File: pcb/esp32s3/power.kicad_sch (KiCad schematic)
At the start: 15 parts, among them J1 USB_C_Receptacle_USB2.0_14P, J2 Battery, Q1 DMG3414U, U2 AZ1117-3.3, U3 USBLC6-2SC6, U4 MCP73831-2-OT

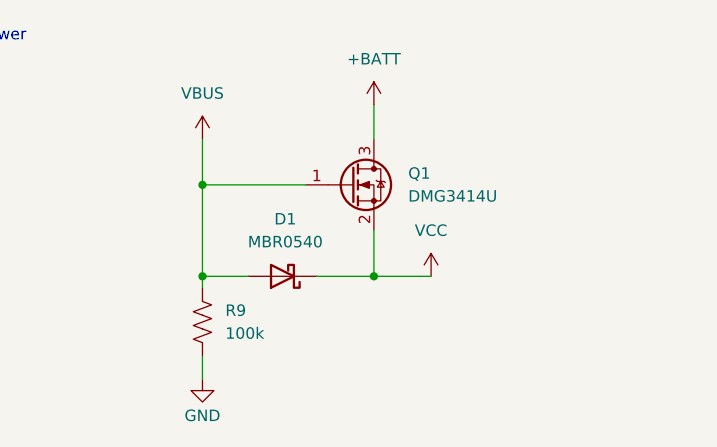
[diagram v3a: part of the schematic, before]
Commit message: fix power circuit
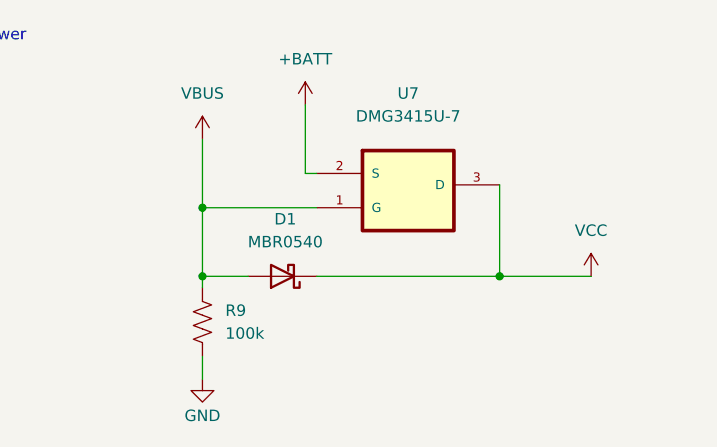
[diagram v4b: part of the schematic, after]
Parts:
- removed Q1: DMG3414U, Package_TO_SOT_SMD:SOT-23, symbol Transistor_FET:DMG3414U
- added U7: DMG3415U-7, DMG3415:SOT95P240X105-3N, symbol DMG3415U-7:DMG3415U-7
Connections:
- net +BATT: now also U7.2 (S)
- net VBUS: now also U7.1 (G)
- net VCC: now also U7.3 (D)
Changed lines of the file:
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@@
 	)
 	(junction
-		(at 248.92 40.64)
-		(diameter 0)
-		(color 0 0 0 0)
-	)
-	(junction
 		(at 57.15 30.48)
 		(diameter 0)
@@
 	)
 	(junction
-		(at 83.82 96.52)
+		(at 262.89 40.64)
+		(diameter 0)
+		(color 0 0 0 0)
+	)
+	(junction
+		(at 229.87 33.02)
 		(diameter 0)
 		(color 0 0 0 0)
 	)
 	(junction
-		(at 229.87 30.48)
+		(at 83.82 96.52)
 		(diameter 0)
 		(color 0 0 0 0)
@@
 	(wire
 		(pts
+			(xy 262.89 40.64) (xy 273.05 40.64)
+		)
+		(stroke
+			(width 0)
+			(type default)
+		)
+	)
+	(wire
+		(pts
 			(xy 234.95 83.82) (xy 240.03 83.82)
 		)
@@
 		)
 	)
+	(wire
+		(pts
+			(xy 229.87 33.02) (xy 229.87 40.64)
+		)
+		(stroke
+			(width 0)
+			(type default)
+		)
+	)
 	(polyline
 		(pts
@@
 	(wire
 		(pts
-			(xy 229.87 25.4) (xy 229.87 30.48)
+			(xy 229.87 25.4) (xy 229.87 33.02)
 		)
 		(stroke
@@
 	(wire
 		(pts
-			(xy 229.87 30.48) (xy 241.3 30.48)
+			(xy 229.87 33.02) (xy 242.57 33.02)
 		)
 		(stroke
@@
 	(wire
 		(pts
-			(xy 248.92 40.64) (xy 248.92 35.56)
-		)
-		(stroke
-			(width 0)
-			(type default)
-		)
-	)
-	(wire
-		(pts
 			(xy 86.36 87.63) (xy 86.36 88.9)
 		)
@@
 	(wire
 		(pts
-			(xy 248.92 40.64) (xy 255.27 40.64)
+			(xy 242.57 40.64) (xy 262.89 40.64)
 		)
 		(stroke
@@
 		)
 	)
-	(wire
+	(polyline
 		(pts
-			(xy 229.87 30.48) (xy 229.87 40.64)
+			(xy 11.938 59.944) (xy 79.756 59.944)
 		)
 		(stroke
@@
 	(wire
 		(pts
-			(xy 242.57 40.64) (xy 248.92 40.64)
+			(xy 241.3 29.21) (xy 242.57 29.21)
 		)
 		(stroke
@@
 		)
 	)
-	(polyline
+	(wire
 		(pts
-			(xy 11.938 59.944) (xy 79.756 59.944)
+			(xy 262.89 30.48) (xy 262.89 40.64)
 		)
 		(stroke
@@
 	(wire
 		(pts
-			(xy 248.92 21.59) (xy 248.92 25.4)
+			(xy 241.3 21.59) (xy 241.3 29.21)
 		)
 		(stroke
@@
 	)
 	(symbol
+		(lib_id "DMG3415U-7:DMG3415U-7")
+		(at 252.73 30.48 0)
+		(unit 1)
+		(exclude_from_sim no)
+		(in_bom yes)
+		(on_board yes)
+		(dnp no)
+		(fields_autoplaced yes)
+		(property "Reference" "U7"
+			(at 252.73 20.32 0)
+			(effects
+				(font
+					(size 1.27 1.27)
+				)
+			)
+		)
+		(property "Value" "DMG3415U-7"
+			(at 252.73 22.86 0)
+			(effects
+				(font
+					(size 1.27 1.27)
+				)
+			)
+		)
+		(property "Footprint" "DMG3415:SOT95P240X105-3N"
+			(at 252.73 30.48 0)
+			(effects
+				(font
+					(size 1.27 1.27)
+				)
+				(justify bottom)
+				(hide yes)
+			)
+		)
+		(property "Datasheet" ""
+			(at 252.73 30.48 0)
+			(effects
+				(font
+					(size 1.27 1.27)
+				)
+				(hide yes)
+			)
+		)
+		(property "Description" ""
+			(at 252.73 30.48 0)
+			(effects
+				(font
+					(size 1.27 1.27)
+				)
+				(hide yes)
+			)
+		)
+		(property "MPN" "DMG3415U-7"
+			(at 252.73 30.48 0)
+			(effects
+				(font
+					(size 1.27 1.27)
+				)
+				(justify bottom)
+				(hide yes)
+			)
+		)
+		(property "OC_FARNELL" "1843688"
+			(at 252.73 30.48 0)
+			(effects
+				(font
+					(size 1.27 1.27)
+				)
+				(justify bottom)
+				(hide yes)
+			)
+		)
+		(property "OC_NEWARK" "12T2026"
+			(at 252.73 30.48 0)
+			(effects
+				(font
+					(size 1.27 1.27)
+				)
+				(justify bottom)
+				(hide yes)
+			)
+		)
+		(property "SUPPLIER" "Diodes Inc"
+			(at 252.73 30.48 0)
+			(effects
+				(font
+					(size 1.27 1.27)
+				)
+				(justify bottom)
+				(hide yes)
+			)
+		)
+		(property "PACKAGE" "SOT-23-3"
+			(at 252.73 30.48 0)
+			(effects
+				(font
+					(size 1.27 1.27)
+				)
+				(justify bottom)
+				(hide yes)
+			)
+		)
+		(pin "1"
+		)
+		(pin "2"
+		)
+		(pin "3"
+		)
+		(instances
+			(project "esp32s3"
+				(path "/834edf73-57a5-43b4-ab36-0b077e93e6d5/ae5309e0-349d-45c3-b1b4-6edffcac73ca"
+					(reference "U7")
+					(unit 1)
+				)
+			)
+		)
+	)
+	(symbol
 		(lib_id "Device:R_US")
 		(at 86.36 92.71 0)
@@
 	(symbol
 		(lib_id "power:VCC")
-		(at 255.27 40.64 0)
+		(at 273.05 40.64 0)
 		(unit 1)
 		(exclude_from_sim no)
@@
 		(fields_autoplaced yes)
 		(property "Reference" "#PWR034"
-			(at 255.27 44.45 0)
+			(at 273.05 44.45 0)
 			(effects
 				(font
@@
 		)
 		(property "Value" "VCC"
-			(at 255.27 35.56 0)
+			(at 273.05 35.56 0)
 			(effects
 				(font
@@
 		)
 		(property "Footprint" ""
-			(at 255.27 40.64 0)
+			(at 273.05 40.64 0)
 			(effects
 				(font
@@
 		)
 		(property "Datasheet" ""
-			(at 255.27 40.64 0)
+			(at 273.05 40.64 0)
 			(effects
 				(font
@@
 		)
 		(property "Description" "Power symbol creates a global label with name \"VCC\""
-			(at 255.27 40.64 0)
+			(at 273.05 40.64 0)
 			(effects
 				(font
@@
 	(symbol
 		(lib_id "power:+BATT")
-		(at 248.92 21.59 0)
+		(at 241.3 21.59 0)
 		(unit 1)
 		(exclude_from_sim no)
@@
 		(fields_autoplaced yes)
 		(property "Reference" "#PWR033"
-			(at 248.92 25.4 0)
+			(at 241.3 25.4 0)
 			(effects
 				(font
@@
 		)
 		(property "Value" "+BATT"
-			(at 248.92 16.51 0)
+			(at 241.3 16.51 0)
 			(effects
 				(font
@@
 		)
 		(property "Footprint" ""
-			(at 248.92 21.59 0)
+			(at 241.3 21.59 0)
 			(effects
 				(font
@@
 		)
 		(property "Datasheet" ""
-			(at 248.92 21.59 0)
+			(at 241.3 21.59 0)
 			(effects
 				(font
@@
 		)
 		(property "Description" "Power symbol creates a global label with name \"+BATT\""
-			(at 248.92 21.59 0)
+			(at 241.3 21.59 0)
 			(effects
 				(font
@@
 					(unit 1)
 				)
-			)
-		)
-	)
-	(symbol
-		(lib_id "Transistor_FET:DMG3414U")
-		(at 246.38 30.48 0)
-		(unit 1)
-		(exclude_from_sim no)
-		(in_bom yes)
-		(on_board yes)
-		(dnp no)
-		(fields_autoplaced yes)
-		(property "Reference" "Q1"
-			(at 252.73 29.2099 0)
-			(effects
-				(font
-					(size 1.27 1.27)
-				)
-				(justify left)
-			)
-		)
-		(property "Value" "DMG3414U"
-			(at 252.73 31.7499 0)
-			(effects
-				(font
-					(size 1.27 1.27)
-				)
-				(justify left)
-			)
-		)
-		(property "Footprint" "Package_TO_SOT_SMD:SOT-23"
-			(at 251.46 32.385 0)
-			(effects
-				(font
-					(size 1.27 1.27)
-					(italic yes)
-				)
-				(justify left)
-				(hide yes)
-			)
-		)
-		(property "Datasheet" "http://www.diodes.com/assets/Datasheets/ds31739.pdf"
-			(at 251.46 34.29 0)
-			(effects
-				(font
-					(size 1.27 1.27)
-				)
-				(justify left)
-				(hide yes)
-			)
-		)
-		(property "Description" "4.2A Id, 20V Vds, N-Channel MOSFET, SOT-23"
-			(at 246.38 30.48 0)
-			(effects
-				(font
-					(size 1.27 1.27)
-				)
-				(hide yes)
-			)
-		)
-		(pin "2"
-		)
-		(pin "3"
-		)
-		(pin "1"
-		)
-		(instances
-			(project "esp32s3"
-				(path "/834edf73-57a5-43b4-ab36-0b077e93e6d5/ae5309e0-349d-45c3-b1b4-6edffcac73ca"
-					(reference "Q1")
-					(unit 1)
-				)

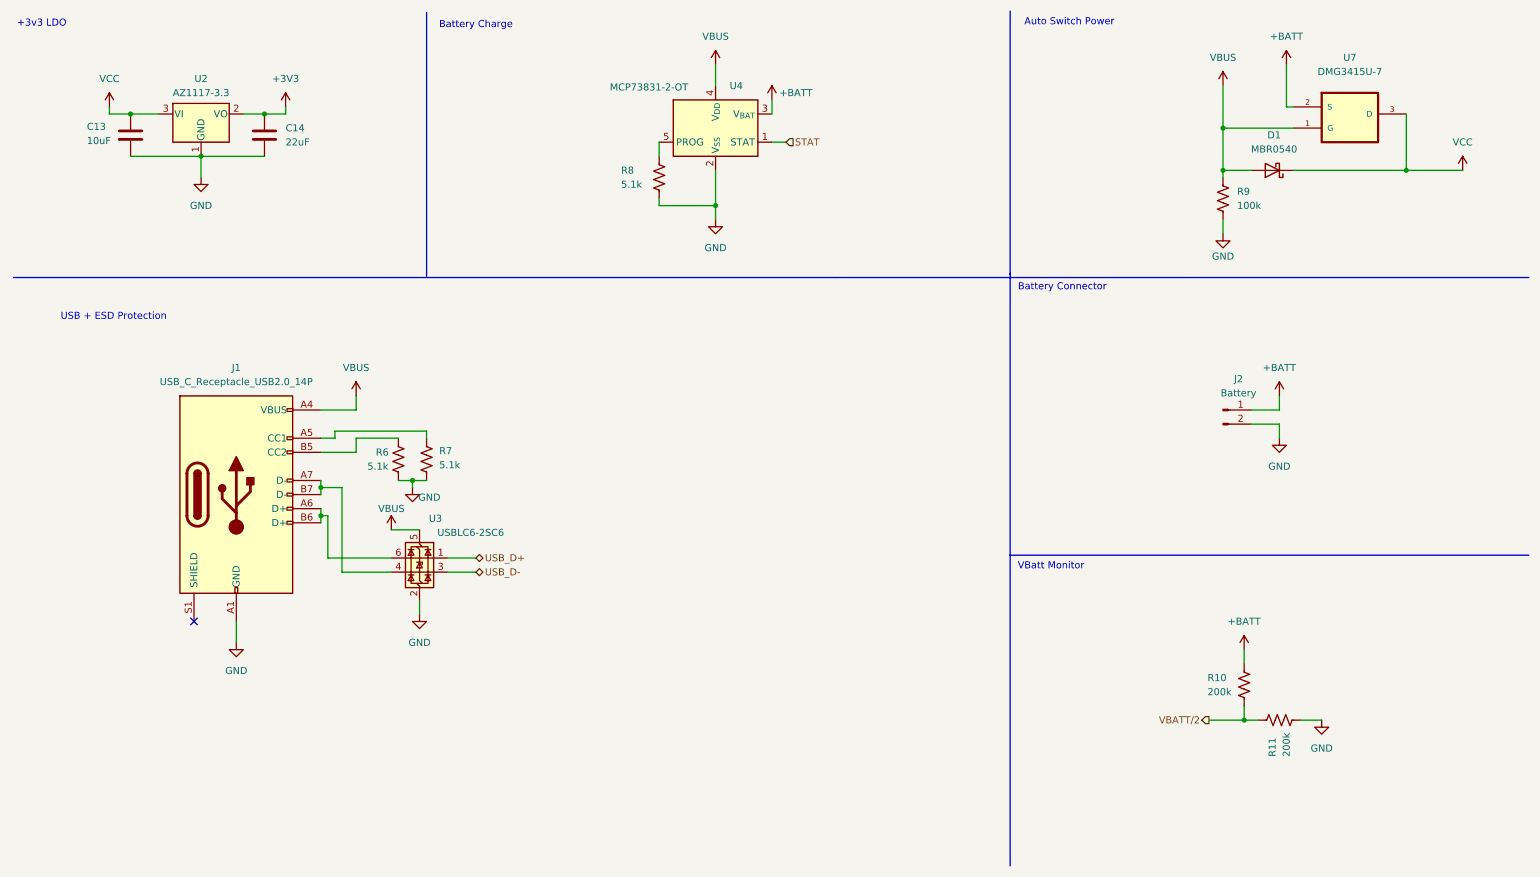
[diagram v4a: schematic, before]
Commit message: added "stm32h7" new pcb and docs
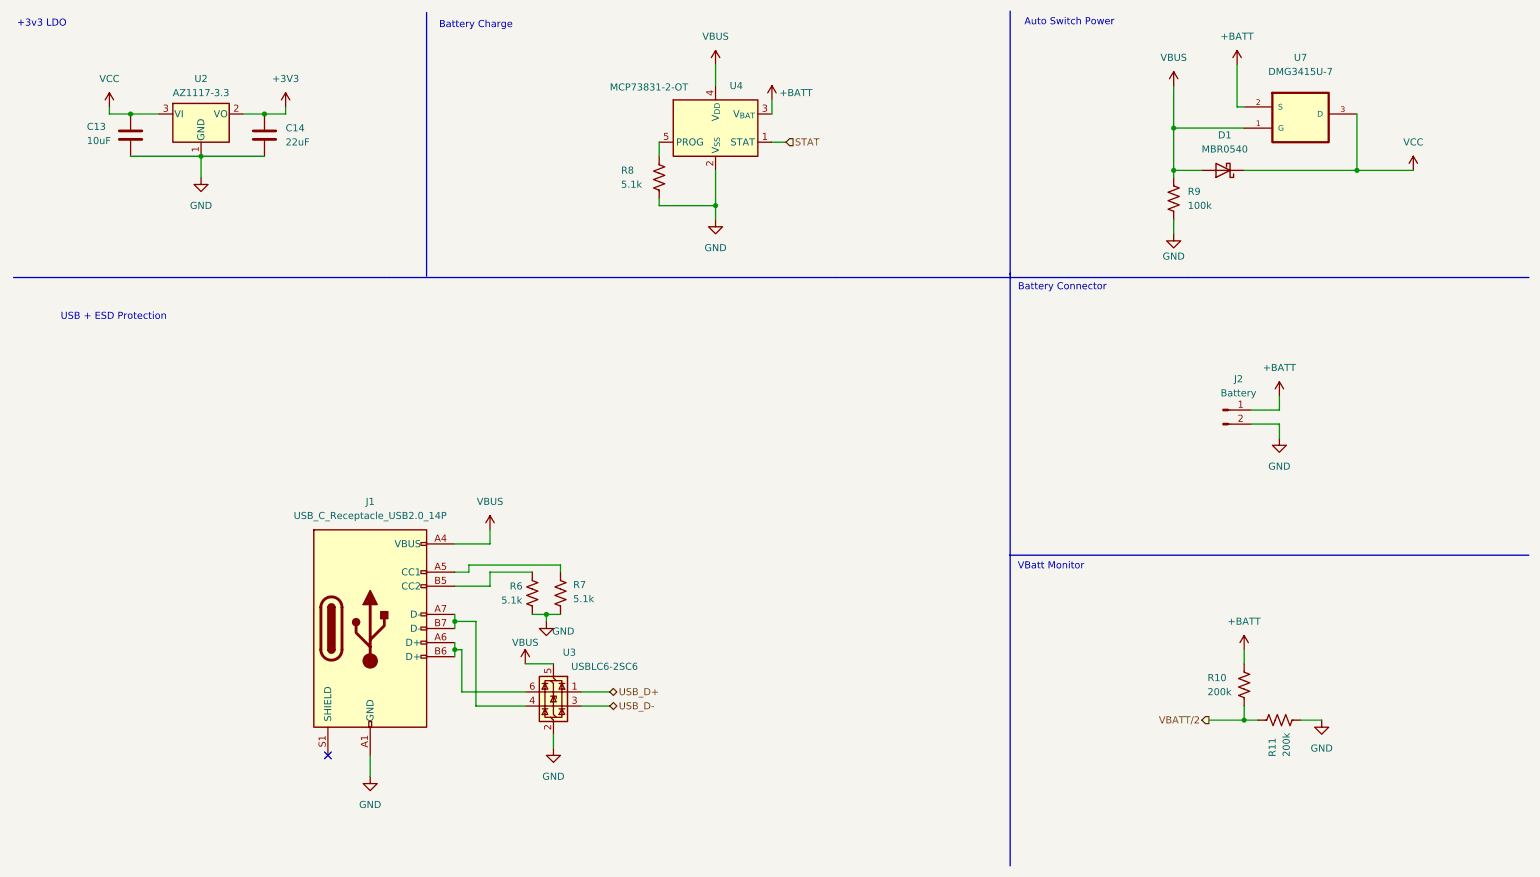
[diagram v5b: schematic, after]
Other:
- moved on the sheet: D1, J1, R6, R7, R9, U3, U7
